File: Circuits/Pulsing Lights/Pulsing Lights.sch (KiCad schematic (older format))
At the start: 11 parts, among them U1 LM555

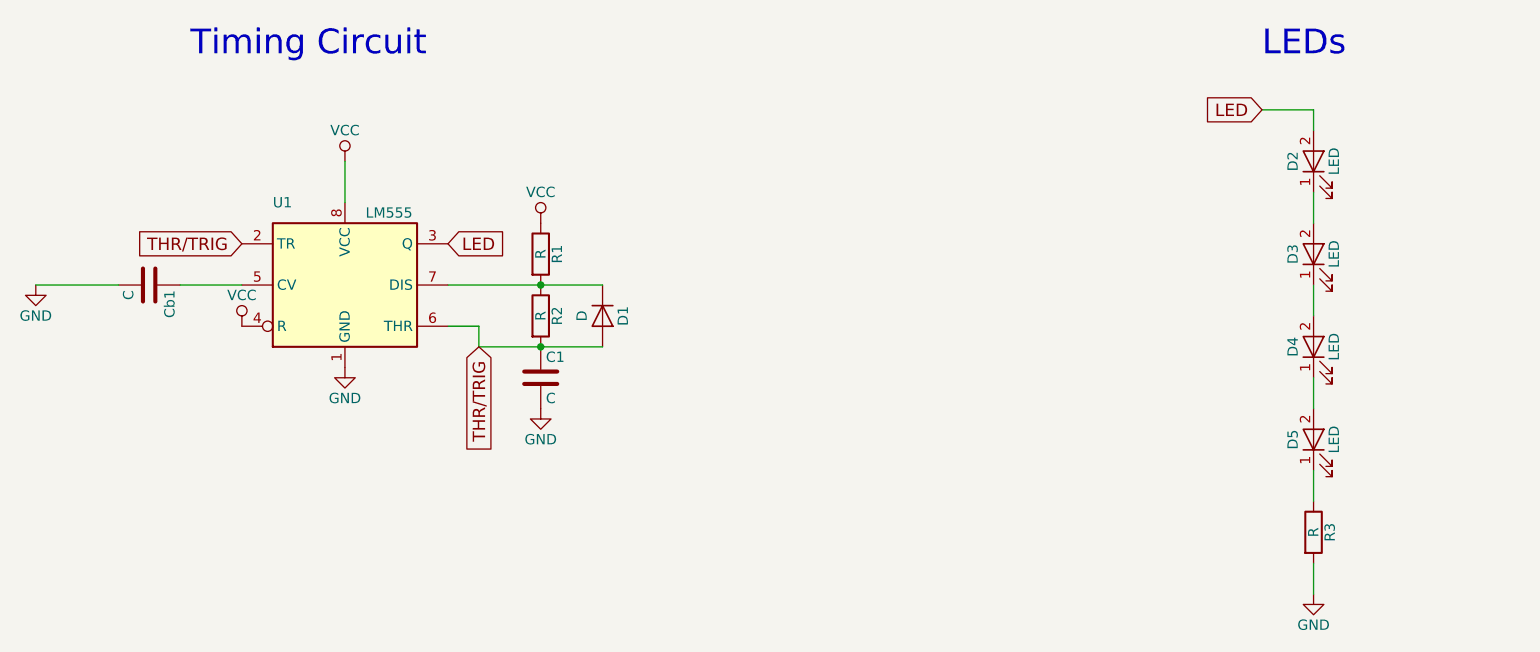
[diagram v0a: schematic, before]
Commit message: Updated the flashing light schematic
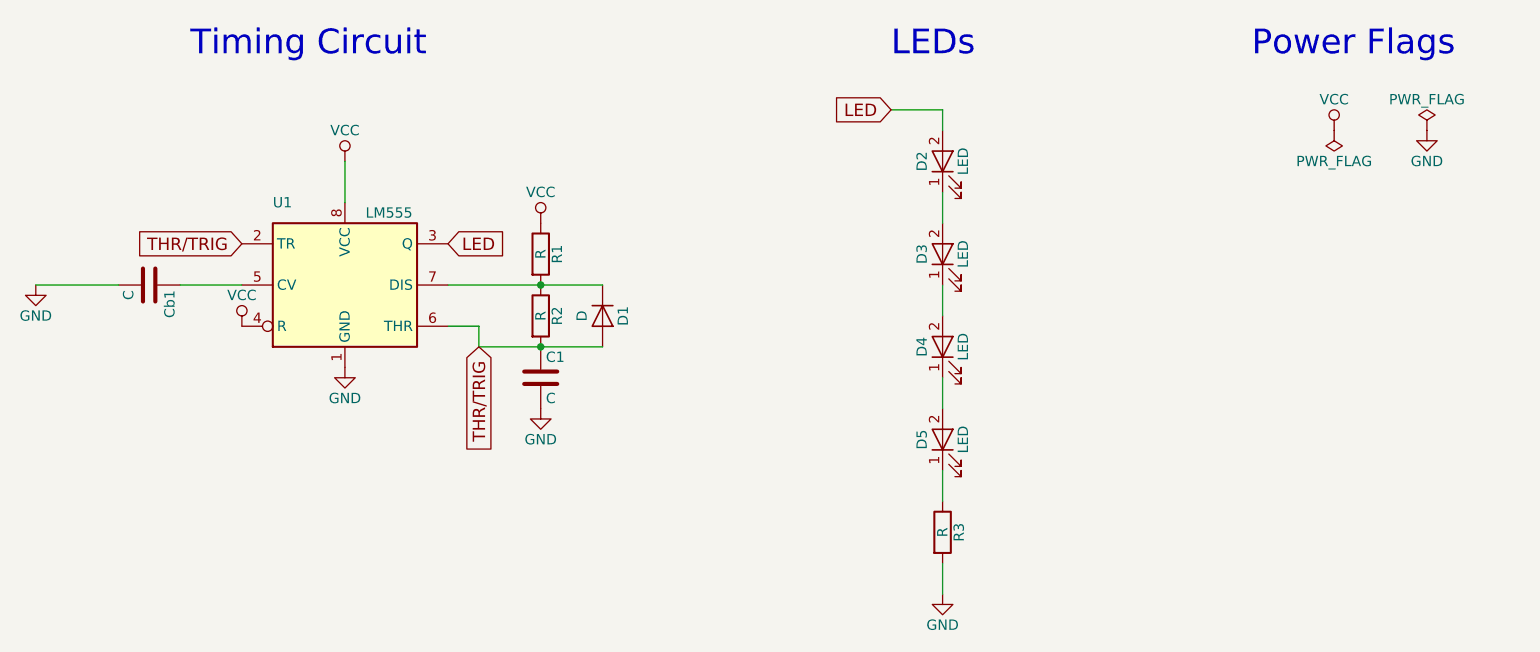
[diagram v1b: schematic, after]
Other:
- note added: "Power Flags"
- moved on the sheet: D2, D3, D4, D5, R3
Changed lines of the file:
@@
 LIBS:contrib
 LIBS:valves
+LIBS:Pulsing Lights-cache
 EELAYER 25 0
 EELAYER END
@@
 $EndComp
 $Comp
-L GND #PWR4
+L GND #PWR01
 U 1 1 5B23C8F1
 P 3300 4400
-F 0 "#PWR4" H 3300 4150 50  0001 C CNN
+F 0 "#PWR01" H 3300 4150 50  0001 C CNN
 F 1 "GND" H 3300 4250 50  0000 C CNN
 F 2 "" H 3300 4400 50  0001 C CNN
@@
 	2200 4000 1800 4000
 $Comp
-L GND #PWR1
+L GND #PWR02
 U 1 1 5B23CFBA
 P 1800 4000
-F 0 "#PWR1" H 1800 3750 50  0001 C CNN
+F 0 "#PWR02" H 1800 3750 50  0001 C CNN
 F 1 "GND" H 1800 3850 50  0000 C CNN
 F 2 "" H 1800 4000 50  0001 C CNN
@@
 $EndComp
 $Comp
-L VCC #PWR3
+L VCC #PWR03
 U 1 1 5B23CFEA
 P 3300 3400
-F 0 "#PWR3" H 3300 3250 50  0001 C CNN
+F 0 "#PWR03" H 3300 3250 50  0001 C CNN
 F 1 "VCC" H 3300 3550 50  0000 C CNN
 F 2 "" H 3300 3400 50  0001 C CNN
@@
 $EndComp
 $Comp
-L VCC #PWR2
+L VCC #PWR04
 U 1 1 5B23D002
 P 2800 4200
-F 0 "#PWR2" H 2800 4050 50  0001 C CNN
+F 0 "#PWR04" H 2800 4050 50  0001 C CNN
 F 1 "VCC" H 2800 4350 50  0000 C CNN
 F 2 "" H 2800 4200 50  0001 C CNN
@@
 $EndComp
 Wire Wire Line
-	3800 4000 4250 4000
-Wire Wire Line
-	4250 4000 4550 4000
+	3800 4000 4550 4000
 Wire Wire Line
 	3800 4200 3950 4200
@@
 	3950 4200 3950 4300
 Wire Wire Line
-	3950 4300 4250 4300
-Wire Wire Line
-	4250 4300 4550 4300
-$Comp
-L VCC #PWR5
+	3950 4300 4550 4300
+$Comp
+L VCC #PWR05
 U 1 1 5B23D407
 P 4250 3700
-F 0 "#PWR5" H 4250 3550 50  0001 C CNN
+F 0 "#PWR05" H 4250 3550 50  0001 C CNN
 F 1 "VCC" H 4250 3850 50  0000 C CNN
 F 2 "" H 4250 3700 50  0001 C CNN
@@
 THR/TRIG
 $Comp
-L GND #PWR6
+L GND #PWR06
 U 1 1 5B23D4CE
 P 4250 4600
-F 0 "#PWR6" H 4250 4350 50  0001 C CNN
+F 0 "#PWR06" H 4250 4350 50  0001 C CNN
 F 1 "GND" H 4250 4450 50  0000 C CNN
 F 2 "" H 4250 4600 50  0001 C CNN
@@
 Text Notes 2550 2900 0    120  ~ 0
 Timing Circuit
-Text Notes 7750 2900 0    120  ~ 0
+Text Notes 5950 2900 0    120  ~ 0
 LEDs
 $Comp
 L LED D2
 U 1 1 5B23DA82
-P 8000 3400
-F 0 "D2" H 8000 3500 50  0000 C CNN
-F 1 "LED" H 8000 3300 50  0000 C CNN
-F 2 "" H 8000 3400 50  0001 C CNN
-F 3 "" H 8000 3400 50  0001 C CNN
-	1    8000 3400
+P 6200 3400
+F 0 "D2" H 6200 3500 50  0000 C CNN
+F 1 "LED" H 6200 3300 50  0000 C CNN
+F 2 "" H 6200 3400 50  0001 C CNN
+F 3 "" H 6200 3400 50  0001 C CNN
+	1    6200 3400
 	0    -1   -1   0
 $EndComp
@@
 L LED D3
 U 1 1 5B23DAFF
-P 8000 3850
-F 0 "D3" H 8000 3950 50  0000 C CNN
-F 1 "LED" H 8000 3750 50  0000 C CNN
-F 2 "" H 8000 3850 50  0001 C CNN
-F 3 "" H 8000 3850 50  0001 C CNN
-	1    8000 3850
+P 6200 3850
+F 0 "D3" H 6200 3950 50  0000 C CNN
+F 1 "LED" H 6200 3750 50  0000 C CNN
+F 2 "" H 6200 3850 50  0001 C CNN
+F 3 "" H 6200 3850 50  0001 C CNN
+	1    6200 3850
 	0    -1   -1   0
 $EndComp
@@
 L LED D4
 U 1 1 5B23DB4E
-P 8000 4300
-F 0 "D4" H 8000 4400 50  0000 C CNN
-F 1 "LED" H 8000 4200 50  0000 C CNN
-F 2 "" H 8000 4300 50  0001 C CNN
-F 3 "" H 8000 4300 50  0001 C CNN
-	1    8000 4300
+P 6200 4300
+F 0 "D4" H 6200 4400 50  0000 C CNN
+F 1 "LED" H 6200 4200 50  0000 C CNN
+F 2 "" H 6200 4300 50  0001 C CNN
+F 3 "" H 6200 4300 50  0001 C CNN
+	1    6200 4300
 	0    -1   -1   0
 $EndComp
@@
 L LED D5
 U 1 1 5B23DCCC
-P 8000 4750
-F 0 "D5" H 8000 4850 50  0000 C CNN
-F 1 "LED" H 8000 4650 50  0000 C CNN
-F 2 "" H 8000 4750 50  0001 C CNN
-F 3 "" H 8000 4750 50  0001 C CNN
-	1    8000 4750
+P 6200 4750
+F 0 "D5" H 6200 4850 50  0000 C CNN
+F 1 "LED" H 6200 4650 50  0000 C CNN
+F 2 "" H 6200 4750 50  0001 C CNN
+F 3 "" H 6200 4750 50  0001 C CNN
+	1    6200 4750
 	0    -1   -1   0
 $EndComp
 Wire Wire Line
-	8000 3550 8000 3700
-Wire Wire Line
-	8000 4000 8000 4150
-Wire Wire Line
-	8000 4450 8000 4600
-Wire Wire Line
-	8000 5050 8000 4900
+	6200 3550 6200 3700
+Wire Wire Line
+	6200 4000 6200 4150
+Wire Wire Line
+	6200 4450 6200 4600
+Wire Wire Line
+	6200 5050 6200 4900
 $Comp
 L R R3
 U 1 1 5B23E01B
-P 8000 5200
-F 0 "R3" V 8080 5200 50  0000 C CNN
-F 1 "R" V 8000 5200 50  0000 C CNN
-F 2 "" V 7930 5200 50  0001 C CNN
-F 3 "" H 8000 5200 50  0001 C CNN
-	1    8000 5200
-	1    0    0    -1
-$EndComp
-Wire Wire Line
-	8000 5350 8000 5500
-$Comp
-L GND #PWR7
+P 6200 5200
+F 0 "R3" V 6280 5200 50  0000 C CNN
+F 1 "R" V 6200 5200 50  0000 C CNN
+F 2 "" V 6130 5200 50  0001 C CNN
+F 3 "" H 6200 5200 50  0001 C CNN
+	1    6200 5200
+	1    0    0    -1
+$EndComp
+Wire Wire Line
+	6200 5350 6200 5500
+$Comp
+L GND #PWR07
 U 1 1 5B23E083
-P 8000 5500
-F 0 "#PWR7" H 8000 5250 50  0001 C CNN
-F 1 "GND" H 8000 5350 50  0000 C CNN
-F 2 "" H 8000 5500 50  0001 C CNN
-F 3 "" H 8000 5500 50  0001 C CNN
-	1    8000 5500
-	1    0    0    -1
-$EndComp
-Wire Wire Line
-	8000 3250 8000 3150
-Wire Wire Line
-	8000 3150 7750 3150
-Text GLabel 7750 3150 0    60   Input ~ 0
+P 6200 5500
+F 0 "#PWR07" H 6200 5250 50  0001 C CNN
+F 1 "GND" H 6200 5350 50  0000 C CNN
+F 2 "" H 6200 5500 50  0001 C CNN
+F 3 "" H 6200 5500 50  0001 C CNN
+	1    6200 5500
+	1    0    0    -1
+$EndComp
+Wire Wire Line
+	6200 3250 6200 3150
+Wire Wire Line
+	6200 3150 5950 3150
+Text GLabel 5950 3150 0    60   Input ~ 0
 LED
+$Comp
+L VCC #PWR08
+U 1 1 5B769520
+P 8100 3250
+F 0 "#PWR08" H 8100 3100 50  0001 C CNN
+F 1 "VCC" H 8100 3400 50  0000 C CNN
+F 2 "" H 8100 3250 50  0001 C CNN
+F 3 "" H 8100 3250 50  0001 C CNN
+	1    8100 3250
+	1    0    0    -1
+$EndComp
+$Comp
+L GND #PWR09
+U 1 1 5B7695B6
+P 8550 3250
+F 0 "#PWR09" H 8550 3000 50  0001 C CNN
+F 1 "GND" H 8550 3100 50  0000 C CNN
+F 2 "" H 8550 3250 50  0001 C CNN
+F 3 "" H 8550 3250 50  0001 C CNN
+	1    8550 3250
+	1    0    0    -1
+$EndComp
+Text Notes 7700 2900 0    120  ~ 0
+Power Flags
+$Comp
+L PWR_FLAG #FLG010
+U 1 1 5B769BA2
+P 8100 3250
+F 0 "#FLG010" H 8100 3325 50  0001 C CNN
+F 1 "PWR_FLAG" H 8100 3400 50  0000 C CNN
+F 2 "" H 8100 3250 50  0001 C CNN
+F 3 "" H 8100 3250 50  0001 C CNN
+	1    8100 3250
+	1    0    0    1
+$EndComp
+$Comp
+L PWR_FLAG #FLG011
+U 1 1 5B769BF7
+P 8550 3250
+F 0 "#FLG011" H 8550 3325 50  0001 C CNN
+F 1 "PWR_FLAG" H 8550 3400 50  0000 C CNN
+F 2 "" H 8550 3250 50  0001 C CNN
+F 3 "" H 8550 3250 50  0001 C CNN
+	1    8550 3250
+	1    0    0    -1
+$EndComp
 $EndSCHEMATC
